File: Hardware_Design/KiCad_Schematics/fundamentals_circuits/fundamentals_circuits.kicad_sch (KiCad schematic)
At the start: 21 parts

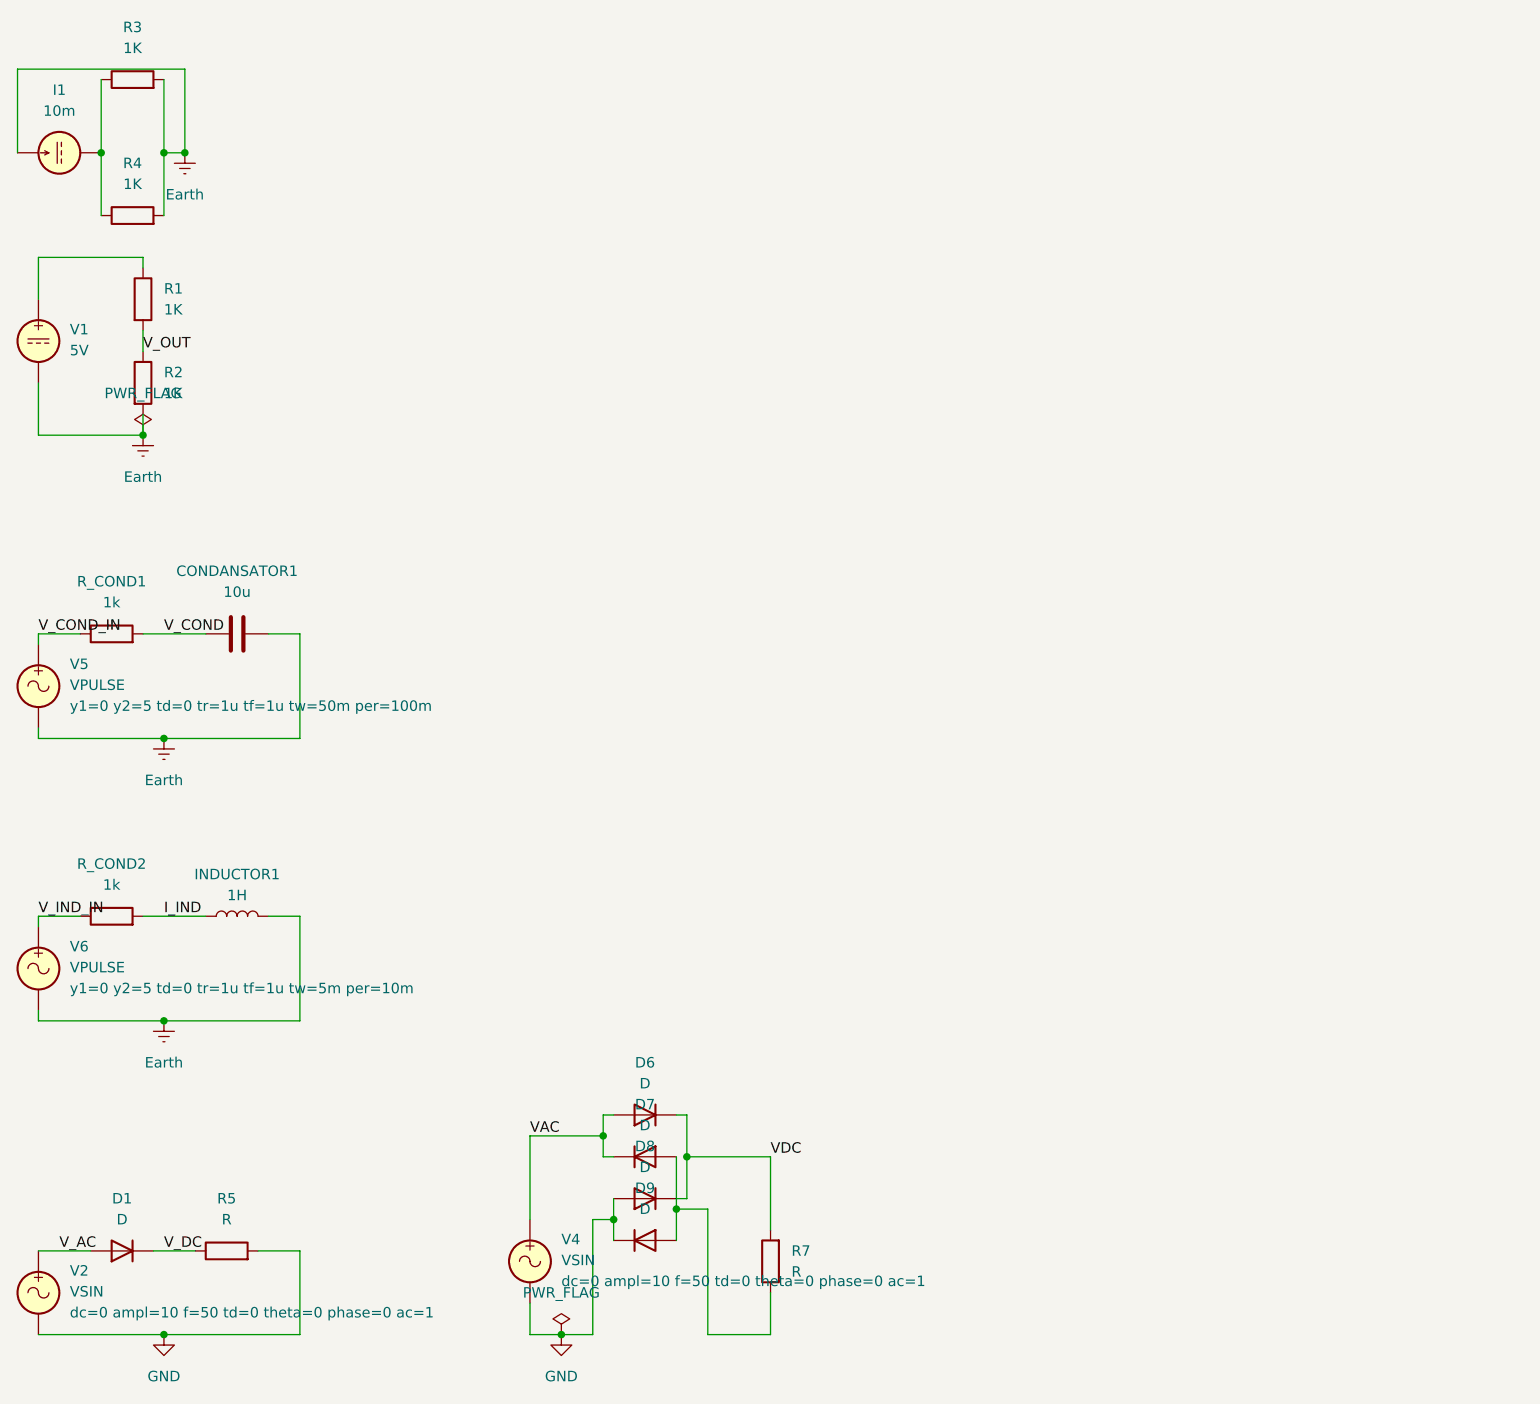
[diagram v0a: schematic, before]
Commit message: PCB designs for fundamental_circuits completed, schematic revised, README added.
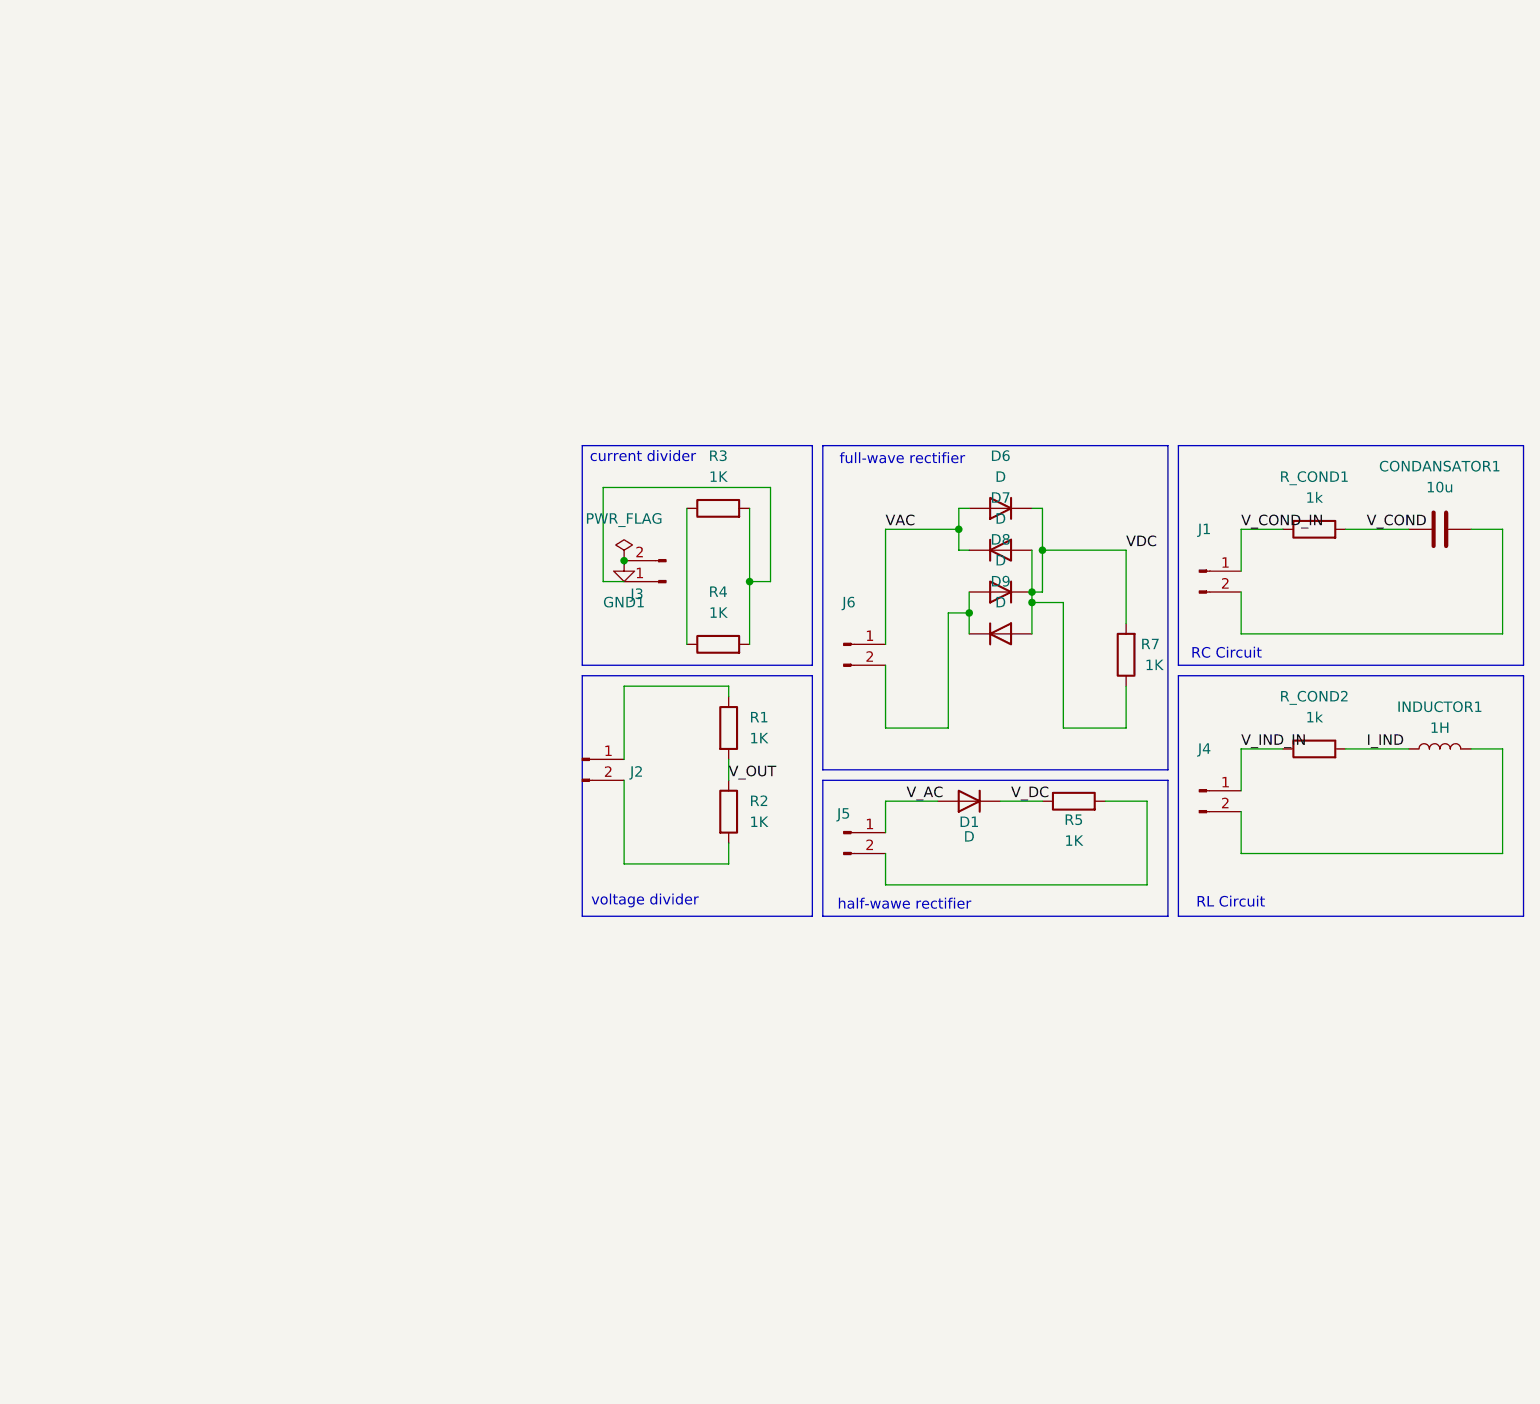
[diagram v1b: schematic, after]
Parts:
- removed I1: 10m, symbol Simulation_SPICE:IDC
- removed V1: 5V, symbol Simulation_SPICE:VDC
- removed V2, V4: VSIN, symbol Simulation_SPICE:VSIN
- removed V5, V6: VPULSE, symbol Simulation_SPICE:VSIN
- added J1, J2, J3, J4, J5, J6: Conn_01x02_Pin, Connector_PinHeader_1.00mm:PinHeader_1x02_P1.00mm_Vertical, symbol Connector:Conn_01x02_Pin
- CONDANSATOR1: footprint (none) -> Capacitor_THT:CP_Radial_D4.0mm_P1.50mm
- D1, D6, D7, D8, D9: footprint (none) -> Diode_THT:D_DO-34_SOD68_P2.54mm_Vertical_AnodeUp
- INDUCTOR1: footprint (none) -> Inductor_THT:L_Axial_L7.0mm_D3.3mm_P2.54mm_Vertical_Fastron_MICC
- R1, R2, R3, R4, R_COND1, R_COND2: footprint (none) -> Resistor_THT:R_Axial_DIN0204_L3.6mm_D1.6mm_P2.54mm_Vertical
- R5, R7: value R -> 1K; footprint (none) -> Resistor_THT:R_Axial_DIN0204_L3.6mm_D1.6mm_P2.54mm_Vertical
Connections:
- net VAC: now also J6.1 (Pin_1)
- net VDC: now also D7.2 (A), D9.2 (A), R7.1
- net V_AC: now also J5.1 (Pin_1)
- net V_COND_IN: now also J1.1 (Pin_1)
- net V_IND_IN: now also J4.1 (Pin_1)
- net at R1.1: now also J2.1 (Pin_1)
- removed net Earth: CONDANSATOR1.2, INDUCTOR1.2, R2.2, R3.2, R4.2
- net GND: no longer names the net of D8.2 (A), D9.1 (K)
- net GND: now also J6.2 (Pin_2); no longer R5.2
- new net: J3.1 (Pin_1), R3.2, R4.2
- new net: CONDANSATOR1.2, J1.2 (Pin_2)
- new net: J5.2 (Pin_2), R5.2
- new net: INDUCTOR1.2, J4.2 (Pin_2)
- new net: J2.2 (Pin_2), R2.2
- new net GND1: J3.2 (Pin_2)
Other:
- note added: "RC Circuit"
- note added: "RL Circuit"
- note added: "current divider"
- note added: "full-wave rectifier"
- note added: "half-wawe rectifier"
- note added: "voltage divider"
- moved on the sheet: CONDANSATOR1, D1, D6, D7, D8, D9, INDUCTOR1, R1, R2, R3, R4, R5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
